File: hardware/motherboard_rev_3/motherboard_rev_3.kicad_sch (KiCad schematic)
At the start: 67 parts, among them J1 Raspberry_Pi_2_3 ANT, J14 USB_C_Receptacle_USB2.0, J2 Conn_ST_STDC14, J3 Battery / Pitot/ Orientation, J4 c02 censor, J5 shaftencorder, J7 SparLoad, J8 lidar, J9 Control Board, Q1 2N7002K, SW1 MCU_RST, U10 TLV76733DRVx, U2 IMU, U3 LM358, U4 GPS module, U5 DHT11(DHT22), U6 STM32F412RETx, U7 nRF24L01-telemetry-INTERIOR, U8 nRF24L01-telemetry-EXTERIOR, U9 DPS310 - barometer, Y1 8M

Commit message: Settled on pin out
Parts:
- removed C15: 10n, Capacitor_SMD:C_0603_1608Metric, symbol Device:C
- removed C16, C3, C4 (x2), C5: 100n, Capacitor_SMD:C_0603_1608Metric, symbol Device:C
- removed H1, H3, H4: MountingHole, MountingHole:MountingHole_2.5mm_Pad, symbol Mechanical:MountingHole
- removed H5, H6, H7, H8: MountingHole, MountingHole:MountingHole_2.7mm_M2.5, symbol Mechanical:MountingHole
- removed J1: Raspberry_Pi_2_3 ANT, Connector_PinSocket_2.54mm:PinSocket_2x20_P2.54mm_Vertical, symbol Connector:Raspberry_Pi_2_3
- removed J3: Battery / Pitot/ Orientation, Connector_JST:JST_EH_B4B-EH-A_1x04_P2.50mm_Vertical, symbol Connector:Conn_01x04_Pin
- removed J4: c02 censor, Connector_JST:JST_EH_B3B-EH-A_1x03_P2.50mm_Vertical, symbol Connector:Conn_01x03_Pin
- removed J5: shaftencorder, Connector_JST:JST_EH_B6B-EH-A_1x06_P2.50mm_Vertical, symbol Connector:Conn_01x06_Pin
- removed J7: SparLoad, Connector_JST:JST_EH_B3B-EH-A_1x03_P2.50mm_Vertical, symbol Connector:Conn_01x03_Pin
- removed J8: lidar, Connector_JST:JST_EH_B4B-EH-A_1x04_P2.50mm_Vertical, symbol Connector:Conn_01x04_Pin
- removed J9: Control Board, Connector_JST:JST_EH_B5B-EH-A_1x05_P2.50mm_Vertical, symbol Connector:Conn_01x05_Pin
- removed JP1: Jumper_3_Open, Jumper:SolderJumper-3_P2.0mm_Open_TrianglePad1.0x1.5mm_NumberLabels, symbol Jumper:Jumper_3_Open
- removed JP4: 5V, Jumper:SolderJumper-2_P1.3mm_Open_RoundedPad1.0x1.5mm, symbol Jumper:Jumper_2_Open
- removed JP5, JP6: Jumper_2_Open, Jumper:SolderJumper-2_P1.3mm_Open_RoundedPad1.0x1.5mm, symbol Jumper:Jumper_2_Open
- removed Q1: 2N7002K, Package_TO_SOT_SMD:SOT-23, symbol Transistor_FET:2N7002K
- removed R1: 100k, Resistor_SMD:R_0603_1608Metric, symbol Device:R
- removed R15: 1k, Resistor_SMD:R_0603_1608Metric, symbol Device:R
- removed R16: 20k, Resistor_SMD:R_0603_1608Metric, symbol Device:R
- removed R17: 470R, Resistor_SMD:R_0603_1608Metric, symbol Device:R
- removed R9: 5.6k, Resistor_SMD:R_0603_1608Metric, symbol Device:R
- removed U10: TLV76733DRVx, Package_SON:WSON-6-1EP_2x2mm_P0.65mm_EP1x1.6mm, symbol Regulator_Linear:TLV76733DRVx
- removed U3: LM358, Package_SO:SOIC-8-1EP_3.9x4.9mm_P1.27mm_EP2.29x3mm, symbol Amplifier_Operational:LM358
- removed U5: DHT11(DHT22), Sensor:Aosong_DHT11_5.5x12.0_P2.54mm, symbol Sensor:DHT11
- removed U6: STM32F412RETx, Package_QFP:LQFP-64_10x10mm_P0.5mm, symbol MCU_ST_STM32F4:STM32F412RETx
- removed U9: DPS310 - barometer, Package_LGA:Bosch_LGA-8_2x2.5mm_P0.65mm_ClockwisePinNumbering, symbol mb_sensors:DPS310
- removed Y1: 8M, Crystal:Resonator_SMD_Murata_CSTxExxV-3Pin_3.0x1.1mm, symbol Device:Resonator
- added C18, C2, C7, C8, C9: 100n, Capacitor_SMD:C_0402_1005Metric, symbol Device:C
- added C19: 1u, Capacitor_SMD:C_0603_1608Metric, symbol Device:C
- added D4: SS34, Diode_SMD:D_SMA, symbol Diode:SS34
- added J3: Conn_01x07, Connector_JST:JST_XH_B7B-XH-A_1x07_P2.50mm_Vertical, symbol Connector_Generic:Conn_01x07
- added J4: Conn_01x03, Connector_JST:JST_XH_B3B-XH-A_1x03_P2.50mm_Vertical, symbol Connector_Generic:Conn_01x03
- added JP1: SolderJumper_3_Open, Jumper:SolderJumper-3_P1.3mm_Open_RoundedPad1.0x1.5mm, symbol Jumper:SolderJumper_3_Open
- added R11: 10k, Resistor_SMD:R_0603_1608Metric, symbol Device:R
- added U2: STM32F412CGUx, Package_DFN_QFN:QFN-48-1EP_7x7mm_P0.5mm_EP5.6x5.6mm, symbol MCU_ST_STM32F4:STM32F412CGUx
- added U4: BMP390, motherboard-footprints:LGA10_BMP390_BOS, symbol mb_sensors:BMP390
- added U5: BME280, Package_LGA:Bosch_LGA-8_2.5x2.5mm_P0.65mm_ClockwisePinNumbering, symbol Sensor:BME280
- added U9: BNO055, Package_LGA:LGA-28_5.2x3.8mm_P0.5mm, symbol Sensor_Motion:BNO055
- added Y1: 20M, symbol Device:Crystal
- C10: renamed from C2; value 4.7u -> 4u7
- C11, C12, C6: footprint Capacitor_SMD:C_0603_1608Metric -> Capacitor_SMD:C_0402_1005Metric; LCSC (none) -> C5448875
- C13, C17: value 0.22u -> 100n; footprint Capacitor_SMD:C_0603_1608Metric -> Capacitor_SMD:C_0402_1005Metric; LCSC (none) -> C5448875
- C3: value 2.2u -> 2u2
- J1: renamed from J2; LCSC (none) -> C2881912
- R10: renamed from R12; value 130R -> 130
- R12: renamed from R11; value 22R -> 22
- R13: renamed from R10; value 22R -> 22
- R14: renamed from R9; value 5.1K -> 5k1
- R15: renamed from R12; value 5.1K -> 5k1
- R4: renamed from R10; value 130R -> 130
- R5: renamed from R11; value 130R -> 130
- U6: renamed from U8; value nRF24L01-telemetry-EXTERIOR -> nRF24L01
- U8: renamed from U7; value nRF24L01-telemetry-INTERIOR -> nRF24L01
- renumbered C2 to C15, C1 to C16, C1 to C4, J14 to J2, R3 to R6, R2 to R7, R13 to R8, R14 to R9, U4 to U1, U2 to U3
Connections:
- net RST is gone; now on net ~{RST}: R7.1, SW1.2
- net +5V: now also D4.1 (K), J4.3 (Pin_3), JP1.1 (A); no longer J2.A4 (VBUS), J2.A9 (VBUS), J2.B4 (VBUS), J2.B9 (VBUS)
- net CO_{2}: now also J4.2 (Pin_2), U2.10 (PA0)
- net ENC1: now also J3.2 (Pin_2), U2.29 (PA8)
- net ENC2: now also J3.3 (Pin_3), U2.26 (PB13)
- net ENC3: now also J3.4 (Pin_4), U2.25 (PB12)
- net GND: now also C6.2, J2.S1 (SHIELD), C18.2, C19.1, C2.2, C7.2, C8.2, C9.2, J3.1 (Pin_1), J4.1 (Pin_1), U2.23 (VSS), U2.35 (VSS), U2.44 (BOOT0), U2.47 (VSS), U2.49 (VSS), U2.8 (VSSA), U4.3 (VSS), U4.5 (SDO), U4.8 (VSS), U4.9 (VSS), U5.1 (GND), U5.7 (GND), U9.17 (COM3), U9.18 (COM2), U9.2 (GND), U9.25 (GNDIO), U9.5 (PS1), U9.6 (PS0); no longer C6.1
- net I2C_{SCK}: now also R9.2, U2.28 (PB15), U4.2 (SCK), U5.4 (SCK), U9.19 (COM1); no longer R8.2
- net I2C_{SDA}: now also R8.2, U2.27 (PB14), U4.4 (SDI), U5.3 (SDI), U9.20 (COM0); no longer R9.2
- net IMU_{CS}: now also U2.38 (PA15)
- net SWCLK: now also U2.37 (PA14)
- net SWDIO: now also U2.34 (PA13)
- net USB+: now also U2.33 (PA12)
- net USB-: now also U2.32 (PA11)
- net ~{RST}: now reaches J1.12 (~{RST})
- net ~{RST}: now also U2.7 (NRST)
- net +3V3: now reaches C13.1
- net +3V3: now also C11.1, C12.1, C15.2, C16.2, C17.1, C3.1, C4.1, C6.1, J1.3 (VCC), R7.2, R8.1, R9.1, U1.1 (3.3V), U1.8 (VIN), U3.5 (VDD_{IO}), U3.8 (VDD), U6.2 (VCC), U8.2 (VCC), C18.1, C2.1, C7.1, C8.1, C9.1, JP1.3 (B), R11.1, U2.24 (VDD), U2.36 (VDD), U2.48 (VDD), U2.9 (VDDA), U4.1 (VDDIO), U4.10 (VDD), U4.6 (CSB), U5.2 (CSB), U5.5 (SDO), U5.6 (VDDIO), U5.8 (VDD), U9.11 (~{RESET}), U9.28 (VDDIO), U9.3 (VDD)
- net at C10.1, R6.2: now also U2.22 (VCAP_1)
- removed net +3.3V: C11.1, C12.1, C15.2, C16.2, C3.1, C4.1, C6.2, J1.3 (VCC), R7.2, R8.1, R9.1, U1.1 (3.3V), U1.8 (VIN), U3.5 (VDD_{IO}), U3.8 (VDD), U6.2 (VCC), U8.2 (VCC)
- net LED1 renamed LED_ERROR
- net LED_ERROR: now also U2.42 (PB6)
- net LED2 renamed LED_IND
- net LED_IND: now also U2.43 (PB7)
- net LED3 renamed LED_HRTBT
- net LED_HRTBT: now also U2.18 (PB0)
- net SPI1MISO renamed RADIO_{MISO}
- net RADIO_{MISO}: now also U2.16 (PA6)
- net SPI1MOSI renamed RADIO_{MOSI}
- net RADIO_{MOSI}: now also U2.17 (PA7)
- net SPI1SCK renamed RADIO_{SCK}
- net RADIO_{SCK}: now also U2.15 (PA5)
- net SPI2MISO renamed IMU_{MISO}
- net IMU_{MISO}: now also U2.40 (PB4)
- net SPI2MOSI renamed IMU_{MOSI}
- net IMU_{MOSI}: now also U2.41 (PB5)
- net SPI2SCK renamed IMU_{SCK}
- net IMU_{SCK}: now also U2.39 (PB3)
- net TELE_{CE}-E renamed RADIO_EXT_CE
- net RADIO_EXT_CE: now also U2.11 (PA1)
- net TELE_{CE}-int renamed RADIO_INT_CE
- net RADIO_INT_CE: now also U2.2 (PC13)
- net TELE_{CS}-E renamed RADIO_EXT_CS
- net RADIO_EXT_CS: now also U2.14 (PA4)
- net TELE_{CS}-int renamed RADIO_INT_CS
- net RADIO_INT_CS: now also U2.19 (PB1)
- net TELE_{IRQ}-E renamed RADIO_EXT_IRQ
- net RADIO_EXT_IRQ: now also U2.4 (PC15)
- net TELE_{IRQ}-int renamed RADIO_INT_IRQ
- net RADIO_INT_IRQ: now also U2.3 (PC14)
- net USART1_{RX} renamed GPS_RX
- net GPS_RX: now also U2.12 (PA2)
- net USART1_{TX} renamed GPS_TX
- net GPS_TX: now also U2.13 (PA3)
- net USART2_{RX} renamed DEBUG_RX
- net DEBUG_RX: now also U2.31 (PA10)
- net USART2_{TX} renamed DEBUG_TX
- net DEBUG_TX: now also U2.30 (PA9)
- new net: J3.7 (Pin_7), JP1.2 (C)
- new net: D4.2 (A), J2.A4 (VBUS), J2.A9 (VBUS), J2.B4 (VBUS), J2.B9 (VBUS)
- new net: R11.2, U9.4 (~{BOOT_LOAD_PIN})
- new net: C19.2, U9.9 (CAP)
- new net: U2.5 (PH0), Y1.2
- new net: U2.6 (PH1), Y1.1
- new net CAN_RX: U2.45 (PB8)
- new net CAN_TX: U2.46 (PB9)
- new net ENC4: J3.5 (Pin_5), U2.21 (PB10)
- new net ENC5: J3.6 (Pin_6), U2.20 (PB2)
- no-connect marks 58 -> 17
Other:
- added sheet CAN (can.kicad_sch)
- added sheet Power (power.kicad_sch)
- note added: "All encoder pins are 5V tolerant"
- note added: "BMP390 is used for high precision pressure to monitor altitude"
- note added: "I^{2}C addess is 0x77"
- note added: "I^{2}C address 0x28"
- note added: "I^{2}C address 0x76"
- moved on the sheet: C10, C15, C16, D1, D2, D3, J1, J2, R10, R12, R14, R15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

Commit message: Completed schematic for rev 3.0 PCB
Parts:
- removed C15, C4: 10n, Capacitor_SMD:C_0603_1608Metric, symbol Device:C
- removed R12, R13: 22, Resistor_SMD:R_0603_1608Metric, symbol Device:R
- removed R8, R9: 10k, Resistor_SMD:R_0603_1608Metric, symbol Device:R
- removed SW1: MCU_RST, Button_Switch_THT:SW_PUSH_6mm_H4.3mm, symbol Switch:SW_Push
- removed Y1: 20M, symbol Device:Crystal
- added R1, R2: 5k1, Resistor_SMD:R_0402_1005Metric, symbol Device:R
- added U8: USBLC6-2SC6, Package_TO_SOT_SMD:SOT-23-6, symbol Power_Protection:USBLC6-2SC6
- added Y1: 20M, Crystal:Resonator_SMD_Murata_CSTxExxV-3Pin_3.0x1.1mm, symbol Device:Resonator
- C11: renamed from C16; footprint Capacitor_SMD:C_0603_1608Metric -> Capacitor_SMD:C_0402_1005Metric; LCSC (none) -> C52923
- C14: renamed from C19; footprint Capacitor_SMD:C_0603_1608Metric -> Capacitor_SMD:C_0402_1005Metric; LCSC (none) -> C52923
- C2: renamed from C3; footprint Capacitor_SMD:C_0603_1608Metric -> Capacitor_SMD:C_0402_1005Metric; LCSC (none) -> C12530
- C4: renamed from C10; LCSC (none) -> C1705
- D1: value LED -> RED; LCSC (none) -> C84256
- D2: value LED -> WHITE; LCSC (none) -> C34499
- D3: value LED -> GREEN; LCSC (none) -> C2293
- J2: LCSC (none) -> C165948
- J3: LCSC (none) -> C144398
- J4: LCSC (none) -> C144394
- R10: renamed from R15; footprint Resistor_SMD:R_0603_1608Metric -> Resistor_SMD:R_0402_1005Metric; LCSC (none) -> C25905
- R3: renamed from R7; footprint Resistor_SMD:R_0603_1608Metric -> Resistor_SMD:R_0402_1005Metric; LCSC (none) -> C723353
- R4: renamed from R6; footprint Resistor_SMD:R_0603_1608Metric -> Resistor_SMD:R_0402_1005Metric; LCSC (none) -> C25530
- R5: renamed from R4; value 130 -> 120; footprint Resistor_SMD:R_0603_1608Metric -> Resistor_SMD:R_0402_1005Metric; LCSC (none) -> C25079
- R6: renamed from R5; value 130 -> 120; footprint Resistor_SMD:R_0603_1608Metric -> Resistor_SMD:R_0402_1005Metric; LCSC (none) -> C25079
- R7: renamed from R10; value 130 -> 120; footprint Resistor_SMD:R_0603_1608Metric -> Resistor_SMD:R_0402_1005Metric; LCSC (none) -> C25079
- R8: renamed from R11; footprint Resistor_SMD:R_0603_1608Metric -> Resistor_SMD:R_0402_1005Metric; LCSC (none) -> C723353
- R9: renamed from R14; footprint Resistor_SMD:R_0603_1608Metric -> Resistor_SMD:R_0402_1005Metric; LCSC (none) -> C25905
- U1, U6: now left out of the parts list
- U2: renamed from U3; value IMU -> ICM-42688; LCSC (none) -> C1850418
- U3: renamed from U2; value STM32F412CGUx -> STM32F412CGU6; LCSC (none) -> C2055817
- U7: renamed from U8; now left out of the parts list
- U9: LCSC (none) -> C93216
- renumbered C2 to C1, C13 to C10, C17 to C12, C18 to C13, C6 to C3, C7 to C5, C8 to C6, C9 to C7, C11 to C8, C12 to C9
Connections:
- net +3V3: now also R1.2, R2.2
- net GND: now also U8.2 (GND), Y1.2
- net USB+: now also U8.4 (I/O2)
- net USB-: now also U8.6 (I/O1)
- net at D4.2 (A), J2.A4 (VBUS), J2.A9 (VBUS)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: now also U8.5 (VBUS)
- net XTAL_1: now reaches U3.5 (PH0)
- net XTAL_1: now also Y1.1
- net XTAL_2: now reaches U3.6 (PH1)
- net XTAL_2: now also Y1.3
- net D+ renamed PORT-
- net PORT-: now also U8.3 (I/O2)
- net D- renamed PORT+
- net PORT+: now also U8.1 (I/O1)
- net I2C_{SCK} renamed SCL
- net SCL: now also R1.1
- net I2C_{SDA} renamed SDA
- net SDA: now also R2.1
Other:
- moved on the sheet: C1, C11, C2, D3, D4, R3, R7

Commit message: Removed LDO and just regulate to 3.3V, also removed off board CO2
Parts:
- removed J3: Conn_01x07, Connector_JST:JST_XH_B7B-XH-A_1x07_P2.50mm_Vertical, symbol Connector_Generic:Conn_01x07
- removed J4: Conn_01x03, Connector_JST:JST_XH_B3B-XH-A_1x03_P2.50mm_Vertical, symbol Connector_Generic:Conn_01x03
- removed JP1: SolderJumper_3_Open, Jumper:SolderJumper-3_P1.3mm_Open_RoundedPad1.0x1.5mm, symbol Jumper:SolderJumper_3_Open
- added J3: EH_S8B-EH, Connector_JST:JST_EH_S8B-EH_1x08_P2.50mm_Horizontal, symbol Connector_Generic:Conn_01x08
- added U10: SCD41-D-R2, Sensor:Sensirion_SCD4x-1EP_10.1x10.1mm_P1.25mm_EP4.8x4.8mm, symbol Sensor_Gas:SCD41-D-R2
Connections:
- net +3V3: now also J3.1 (Pin_1), U10.19 (VDD), U10.7 (VDD); no longer U1.1 (3.3V)
- net ENC1: now also J3.2 (Pin_2)
- net ENC2: now also J3.3 (Pin_3)
- net ENC3: now also J3.4 (Pin_4)
- net ENC4: now also J3.5 (Pin_5)
- net ENC5: now also J3.6 (Pin_6)
- net GND: now also D1.1 (K), D2.1 (K), D3.1 (K), J3.8 (Pin_8), U10.20 (GND), U10.21 (GND), U10.6 (GND); no longer R5.1, R6.1, R7.2
- net LED_ERROR: now also R5.2; no longer D1.2 (A)
- net LED_HRTBT: now also R7.2; no longer D3.2 (A)
- net LED_IND: now also R6.2; no longer D2.2 (A)
- net PORT+: now also J2.A6 (D+), J2.B6 (D+), U8.3 (I/O2); no longer J2.A7 (D-), J2.B7 (D-), U8.1 (I/O1)
- net PORT-: now also J2.A7 (D-), J2.B7 (D-), U8.1 (I/O1); no longer J2.A6 (D+), J2.B6 (D+), U8.3 (I/O2)
- net SCL: now also U10.9 (SCL)
- net SDA: now also U10.10 (SDA)
- net at R7.1: now also D3.2 (A); no longer D3.1 (K)
- net +5V renamed +BATT
- net CO_{2} renamed PWM_{IN}
- net PWM_{IN}: now also J3.7 (Pin_7)
- new net: D2.2 (A), R6.1
- new net: D1.2 (A), R5.1
- no-connect marks 17 -> 18
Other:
- note added: "Allows USB power draw to be monitored"
- moved on the sheet: D1, D2, D3, R5, R6, R7, U6, U7

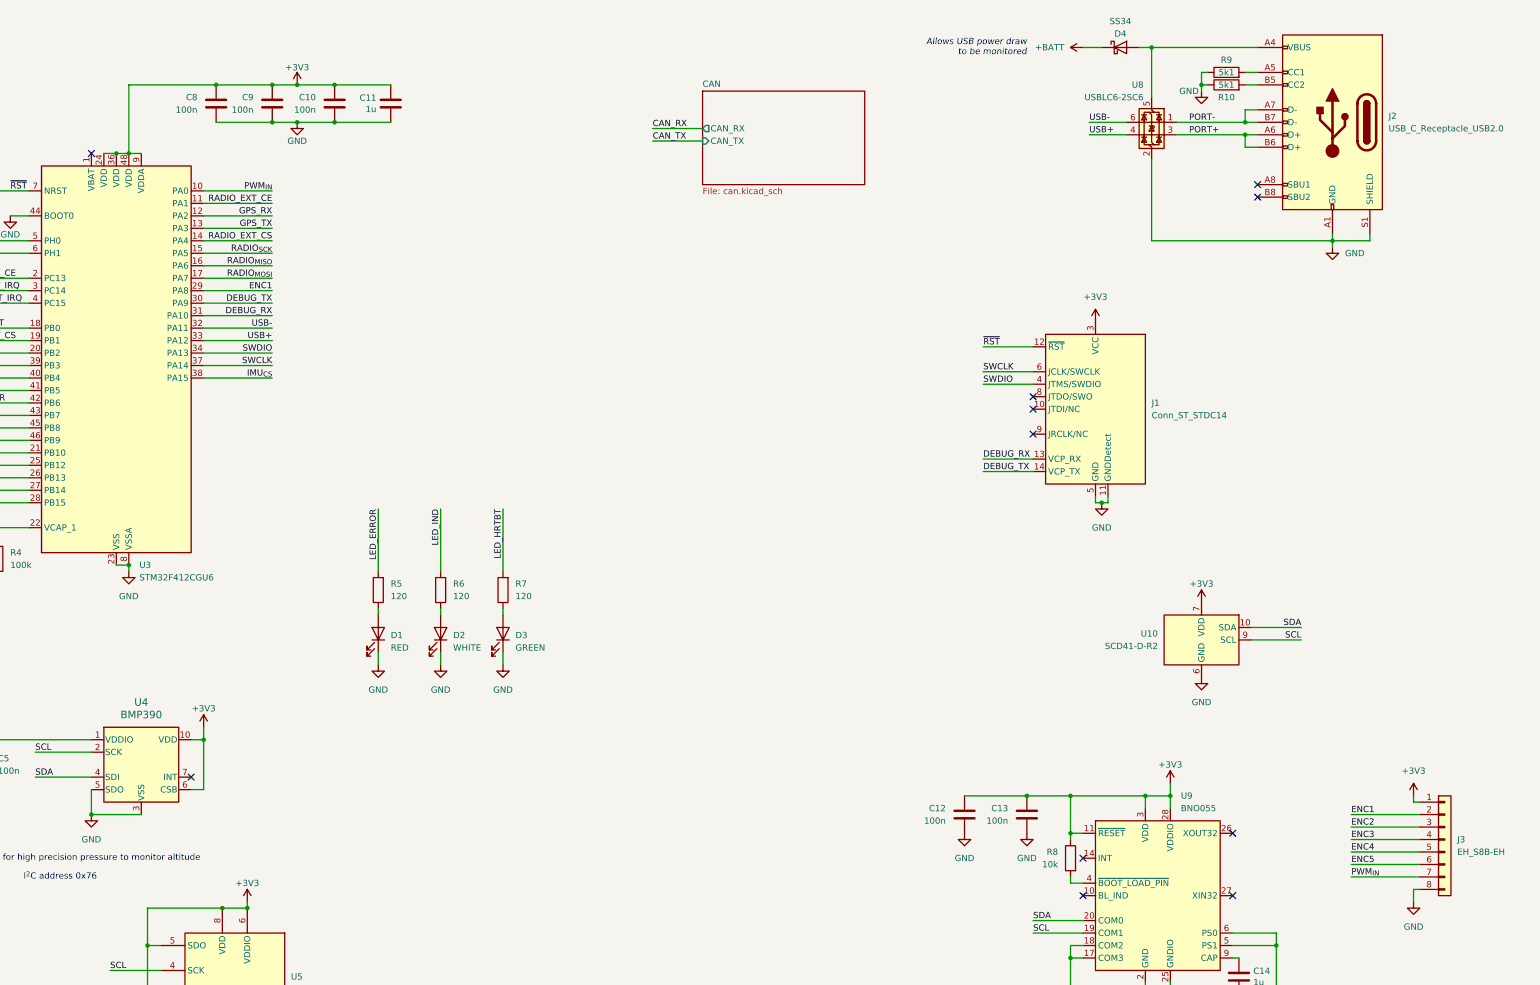
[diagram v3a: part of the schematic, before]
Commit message: Completed layout except for radio modules
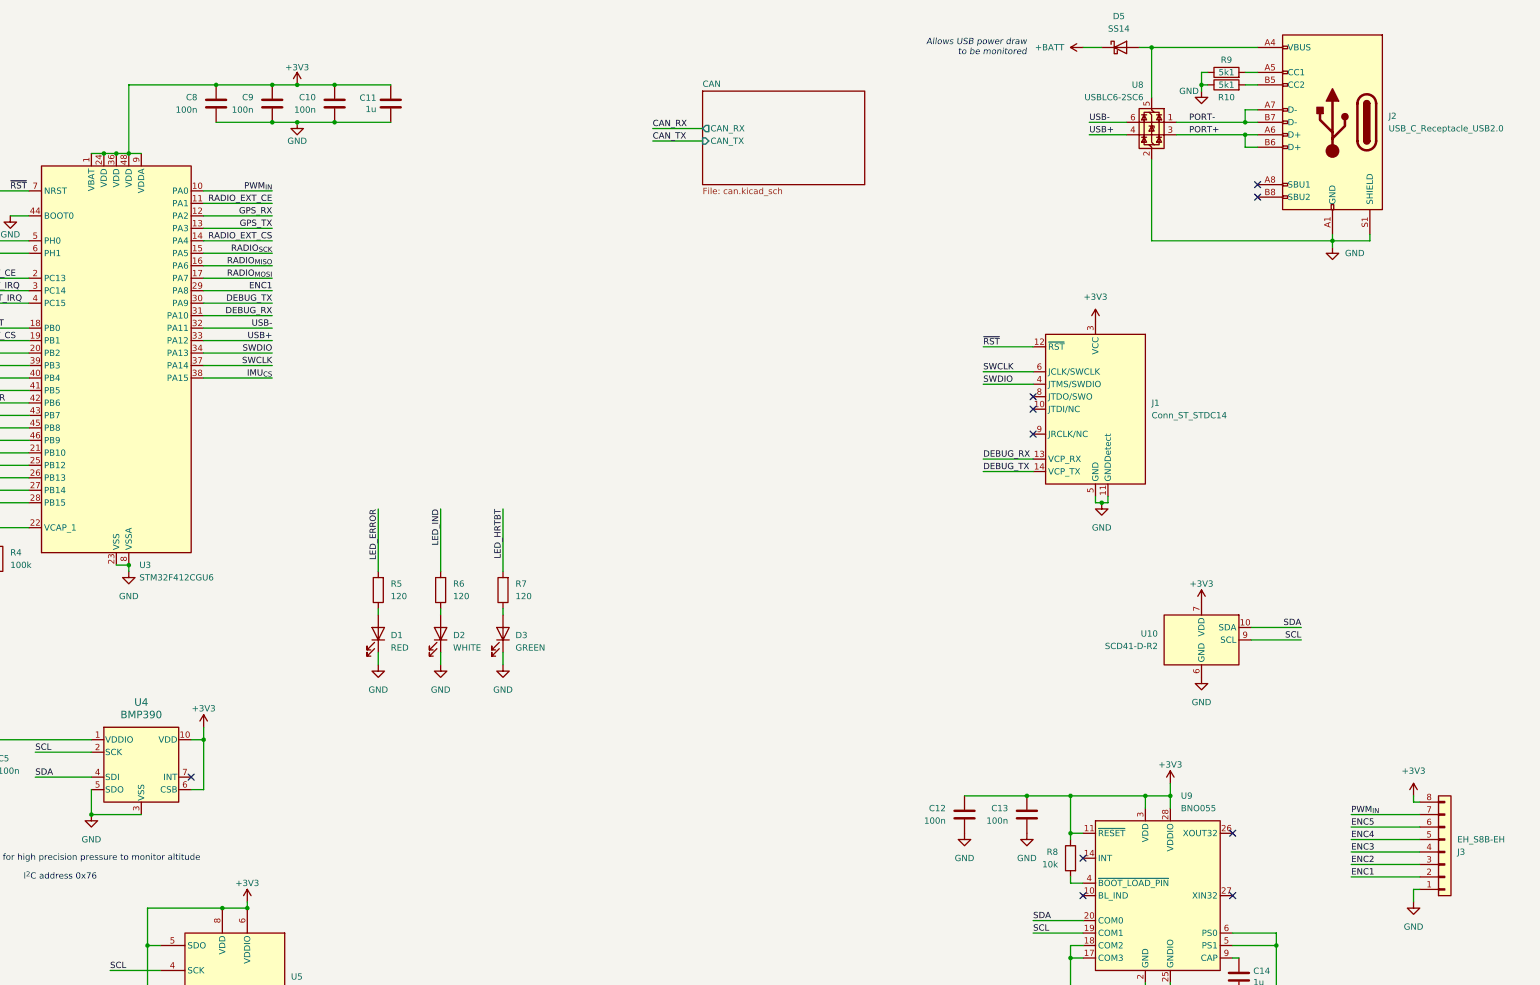
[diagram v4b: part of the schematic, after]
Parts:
- removed D4: SS34, Diode_SMD:D_SMA, symbol Diode:SS34
- added D5: SS14, Diode_SMD:D_SOD-123F, symbol Diode:SS14
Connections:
- net +3V3: now also J3.8 (Pin_8), U3.1 (VBAT); no longer J3.1 (Pin_1)
- net +BATT: now also D5.1 (K)
- net GND: now also J3.1 (Pin_1); no longer J3.8 (Pin_8)
- net at J2.A4 (VBUS), J2.A9 (VBUS), J2.B4 (VBUS)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: now also D5.2 (A)
- no-connect marks 18 -> 17
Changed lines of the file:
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@@
 		(color 0 0 0 0)
 	)
-	(no_connect
-		(at 313.69 99.06)
+	(junction
+		(at 124.46 49.53)
+		(diameter 0)
+		(color 0 0 0 0)
 	)
 	(no_connect
-		(at 121.92 49.53)
+		(at 313.69 99.06)
 	)
 	(no_connect
@@
 	(wire
 		(pts
+			(xy 121.92 49.53) (xy 124.46 49.53)
+		)
+		(stroke
+			(width 0)
+			(type default)
+		)
+	)
+	(wire
+		(pts
 			(xy 148.59 203.2) (xy 153.67 203.2)
 		)
@@
 	)
 	(label "ENC5"
-		(at 378.46 194.31 0)
+		(at 378.46 186.69 0)
 		(effects
 			(font
@@
 	)
 	(label "ENC1"
-		(at 378.46 184.15 0)
+		(at 378.46 196.85 0)
 		(effects
 			(font
@@
 	)
 	(label "ENC3"
-		(at 378.46 189.23 0)
+		(at 378.46 191.77 0)
 		(effects
 			(font
@@
 	)
 	(label "ENC4"
-		(at 378.46 191.77 0)
+		(at 378.46 189.23 0)
 		(effects
 			(font
@@
 	)
 	(label "ENC2"
-		(at 378.46 186.69 0)
+		(at 378.46 194.31 0)
 		(effects
 			(font
@@
 	)
 	(label "PWM_{IN}"
-		(at 378.46 196.85 0)
+		(at 378.46 184.15 0)
 		(effects
 			(font
@@
 	)
 	(symbol
-		(lib_id "Diode:SS34")
-		(at 331.47 27.94 0)
-		(unit 1)
-		(exclude_from_sim no)
-		(in_bom yes)
-		(on_board yes)
-		(dnp no)
-		(property "Reference" "D4"
-			(at 331.47 25.146 0)
-			(effects
-				(font
-					(size 1.27 1.27)
-				)
-			)
-		)
-		(property "Value" "SS34"
-			(at 331.47 22.606 0)
-			(effects
-				(font
-					(size 1.27 1.27)
-				)
-			)
-		)
-		(property "Footprint" "Diode_SMD:D_SMA"
-			(at 331.47 32.385 0)
-			(effects
-				(font
-					(size 1.27 1.27)
-				)
-				(hide yes)
-			)
-		)
-		(property "Datasheet" "https://www.vishay.com/docs/88751/ss32.pdf"
-			(at 331.47 27.94 0)
-			(effects
-				(font
-					(size 1.27 1.27)
-				)
-				(hide yes)
-			)
-		)
-		(property "Description" "40V 3A Schottky Diode, SMA"
-			(at 331.47 27.94 0)
-			(effects
-				(font
-					(size 1.27 1.27)
-				)
-				(hide yes)
-			)
-		)
-		(property "LCSC" "C8678"
-			(at 331.47 27.94 0)
-			(effects
-				(font
-					(size 1.27 1.27)
-				)
-				(hide yes)
-			)
-		)
-		(pin "1"
-		)
-		(pin "2"
-		)
-		(instances
-			(project "motherboard_rev_3"
-				(path "/39c7ec0f-0a05-4172-b48a-dcc9b63f77ff"
-					(reference "D4")
-					(unit 1)
-				)
-			)
-		)
-	)
-	(symbol
 		(lib_id "Device:C")
 		(at 44.45 242.57 0)
@@
 	)
 	(symbol
+		(lib_id "Diode:SS14")
+		(at 331.47 27.94 0)
+		(unit 1)
+		(exclude_from_sim no)
+		(in_bom yes)
+		(on_board yes)
+		(dnp no)
+		(fields_autoplaced yes)
+		(property "Reference" "D5"
+			(at 331.1525 21.59 0)
+			(effects
+				(font
+					(size 1.27 1.27)
+				)
+			)
+		)
+		(property "Value" "SS14"
+			(at 331.1525 24.13 0)
+			(effects
+				(font
+					(size 1.27 1.27)
+				)
+			)
+		)
+		(property "Footprint" "Diode_SMD:D_SOD-123F"
+			(at 331.47 32.385 0)
+			(effects
+				(font
+					(size 1.27 1.27)
+				)
+				(hide yes)
+			)
+		)
+		(property "Datasheet" "https://www.vishay.com/docs/88746/ss12.pdf"
+			(at 331.47 27.94 0)
+			(effects
+				(font
+					(size 1.27 1.27)
+				)
+				(hide yes)
+			)
+		)
+		(property "Description" "40V 1A Schottky Diode, SMA"
+			(at 331.47 27.94 0)
+			(effects
+				(font
+					(size 1.27 1.27)
+				)
+				(hide yes)
+			)
+		)
+		(property "LCSC" "C2909920"
+			(at 331.47 27.94 0)
+			(effects
+				(font
+					(size 1.27 1.27)
+				)
+				(hide yes)
+			)
+		)
+		(pin "1"
+		)
+		(pin "2"
+		)
+		(instances
+			(project ""
+				(path "/39c7ec0f-0a05-4172-b48a-dcc9b63f77ff"
+					(reference "D5")
+					(unit 1)
+				)
+			)
+		)
+	)
+	(symbol
 		(lib_id "Device:C")
 		(at 96.52 132.08 0)
@@
 	(symbol
 		(lib_id "Connector_Generic:Conn_01x08")
-		(at 397.51 189.23 0)
+		(at 397.51 191.77 0)
+		(mirror x)
 		(unit 1)
 		(exclude_from_sim no)
@@
 		(on_board yes)
 		(dnp no)
-		(fields_autoplaced yes)
 		(property "Reference" "J3"
-			(at 400.05 189.2299 0)
+			(at 400.05 191.7701 0)
 			(effects
 				(font
@@
 		)
 		(property "Value" "EH_S8B-EH"
-			(at 400.05 191.7699 0)
+			(at 400.05 189.2301 0)
 			(effects
 				(font
@@
 		)
 		(property "Footprint" "Connector_JST:JST_EH_S8B-EH_1x08_P2.50mm_Horizontal"
-			(at 397.51 189.23 0)
+			(at 397.51 191.77 0)
 			(effects
 				(font
@@
 		)
 		(property "Datasheet" "~"
-			(at 397.51 189.23 0)
+			(at 397.51 191.77 0)
 			(effects
 				(font
@@
 		)
 		(property "Description" "Generic connector, single row, 01x08, script generated (kicad-library-utils/schlib/autogen/connector/)"
-			(at 397.51 189.23 0)
+			(at 397.51 191.77 0)
 			(effects
 				(font
@@
 		)
 		(property "LCSC" "C265106"
-			(at 397.51 189.23 0)
+			(at 397.51 191.77 0)
 			(effects
 				(font
@@
 		)
 		(instances
-			(project ""
+			(project "motherboard_rev_3"
 				(path "/39c7ec0f-0a05-4172-b48a-dcc9b63f77ff"
 					(reference "J3")
